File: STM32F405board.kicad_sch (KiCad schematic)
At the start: 24 parts

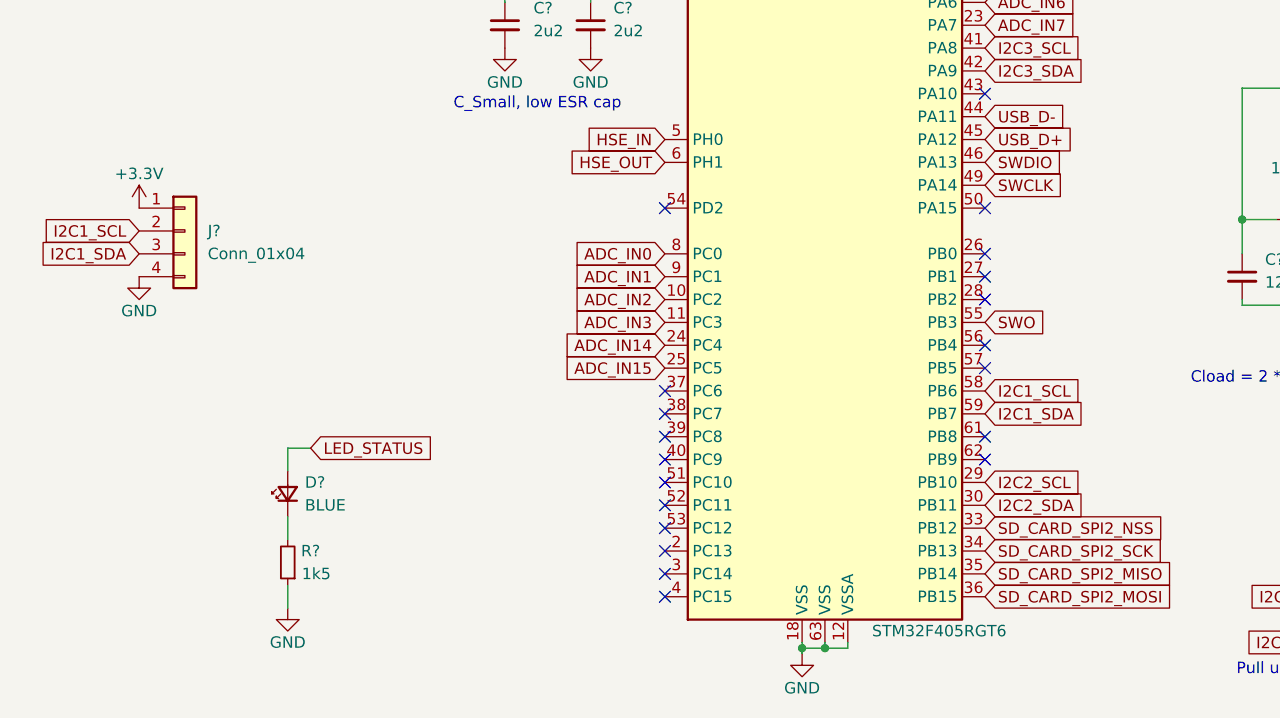
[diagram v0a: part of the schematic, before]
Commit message: Final Schematic
Final Schematic. PC104 pins not assigned.
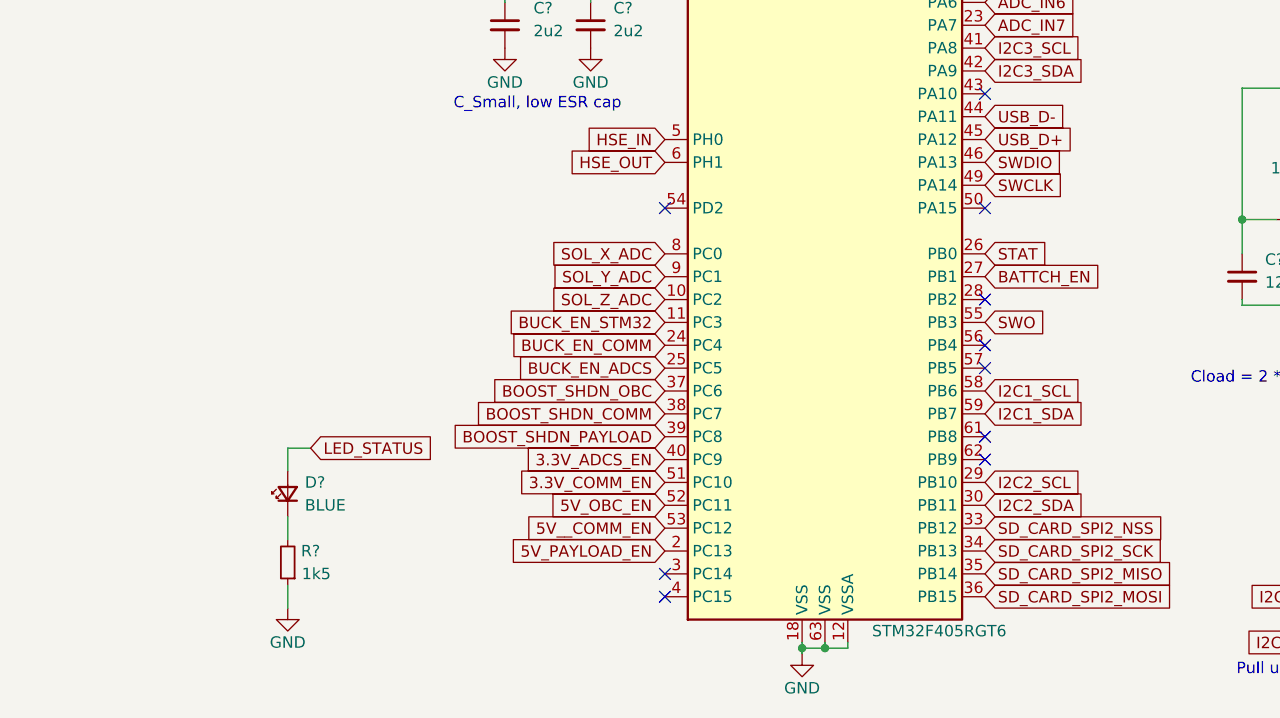
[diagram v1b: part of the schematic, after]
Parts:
- removed J?: Conn_01x04, Connector_Molex:Molex_PicoBlade_53048-0410_1x04_P1.25mm_Horizontal, symbol Connector_Generic:Conn_01x04
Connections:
- net 5V_PAYLOAD_EN: now reaches U?.2 (PC13)
- net STAT: now reaches U?.26 (PB0)
- net BATTCH_EN: now reaches U?.27 (PB1)
- net BOOST_SHDN_OBC: now reaches U?.37 (PC6)
- net BOOST_SHDN_COMM: now reaches U?.38 (PC7)
- net BOOST_SHDN_PAYLOAD: now reaches U?.39 (PC8)
- net 3.3V_ADCS_EN: now reaches U?.40 (PC9)
- net 3.3V_COMM_EN: now reaches U?.51 (PC10)
- net 5V_OBC_EN: now reaches U?.52 (PC11)
- net 5V__COMM_EN: now reaches U?.53 (PC12)
- net ADC_IN0 renamed SOL_X_ADC
- net ADC_IN1 renamed SOL_Y_ADC
- net ADC_IN14 renamed BUCK_EN_COMM
- net ADC_IN15 renamed BUCK_EN_ADCS
- net ADC_IN2 renamed SOL_Z_ADC
- net ADC_IN3 renamed BUCK_EN_STM32
- no-connect marks 24 -> 14

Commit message: Ready to rearrange
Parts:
- J?: footprint Connector_PinHeader_1.27mm:PinHeader_2x05_P1.27mm_Vertical_SMD -> Connector_PinHeader_1.00mm:PinHeader_2x05_P1.00mm_Vertical_SMD
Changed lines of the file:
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@@
       (effects (font (size 1.27 1.27)))
     )
-    (property "Footprint" "Connector_PinHeader_1.27mm:PinHeader_2x05_P1.27mm_Vertical_SMD" (at 233.68 100.33 0)
+    (property "Footprint" "Connector_PinHeader_1.00mm:PinHeader_2x05_P1.00mm_Vertical_SMD" (at 233.68 100.33 0)
       (effects (font (size 1.27 1.27)) hide)
     )

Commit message: updates
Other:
- moved on the sheet: J?
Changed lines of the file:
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@@
   (junction (at 127 61.595) (diameter 0) (color 0 0 0 0)
   )
-  (junction (at 226.695 100.33) (diameter 0) (color 0 0 0 0)
+  (junction (at 127.635 38.1) (diameter 0) (color 0 0 0 0)
   )
   (junction (at 132.08 154.305) (diameter 0) (color 0 0 0 0)
   )
-  (junction (at 226.695 105.41) (diameter 0) (color 0 0 0 0)
+  (junction (at 127.635 43.18) (diameter 0) (color 0 0 0 0)
   )
   (junction (at 134.62 61.595) (diameter 0) (color 0 0 0 0)
@@
   (junction (at 179.07 33.655) (diameter 0) (color 0 0 0 0)
   )
-  (no_connect (at 228.6 102.87))
+  (no_connect (at 129.54 40.64))
   (no_connect (at 149.86 130.81))
   (no_connect (at 149.86 120.65))
@@
   (no_connect (at 114.3 148.59))
   (no_connect (at 149.86 67.31))
-  (no_connect (at 241.3 102.87))
+  (no_connect (at 142.24 40.64))
   (no_connect (at 149.86 123.19))
   (no_connect (at 149.86 69.85))
@@
     (stroke (width 0) (type default))
   )
-  (wire (pts (xy 226.695 93.345) (xy 226.695 95.25))
+  (wire (pts (xy 127.635 31.115) (xy 127.635 33.02))
     (stroke (width 0) (type default))
   )
@@
     (stroke (width 0) (type default))
   )
-  (wire (pts (xy 226.695 95.25) (xy 228.6 95.25))
+  (wire (pts (xy 127.635 33.02) (xy 129.54 33.02))
     (stroke (width 0) (type default))
   )
@@
     (stroke (width 0) (type default))
   )
-  (wire (pts (xy 226.695 100.33) (xy 226.695 105.41))
+  (wire (pts (xy 127.635 38.1) (xy 127.635 43.18))
     (stroke (width 0) (type default))
   )
@@
     (stroke (width 0) (type default))
   )
-  (wire (pts (xy 228.6 97.79) (xy 226.695 97.79))
-    (stroke (width 0) (type default))
-  )
-  (wire (pts (xy 228.6 105.41) (xy 226.695 105.41))
+  (wire (pts (xy 129.54 35.56) (xy 127.635 35.56))
+    (stroke (width 0) (type default))
+  )
+  (wire (pts (xy 129.54 43.18) (xy 127.635 43.18))
     (stroke (width 0) (type default))
   )
@@
     (stroke (width 0) (type default))
   )
-  (wire (pts (xy 226.695 97.79) (xy 226.695 100.33))
+  (wire (pts (xy 127.635 35.56) (xy 127.635 38.1))
     (stroke (width 0) (type default))
   )
@@
     (stroke (width 0) (type default))
   )
-  (wire (pts (xy 226.695 105.41) (xy 226.695 107.315))
+  (wire (pts (xy 127.635 43.18) (xy 127.635 45.085))
     (stroke (width 0) (type default))
   )
@@
     (stroke (width 0) (type default))
   )
-  (wire (pts (xy 228.6 100.33) (xy 226.695 100.33))
+  (wire (pts (xy 129.54 38.1) (xy 127.635 38.1))
     (stroke (width 0) (type default))
   )
@@
     (effects (font (size 1.27 1.27)) (justify left bottom))
   )
-  (text "DEBUG connector" (at 228.6 116.84 0)
+  (text "DEBUG connector" (at 129.54 54.61 0)
     (effects (font (size 1.27 1.27)) (justify left bottom))
   )
@@
     )
   )
-  (global_label "SWDIO" (shape input) (at 241.3 95.25 0) (fields_autoplaced)
-    (effects (font (size 1.27 1.27)) (justify left))
-    (property "Intersheetrefs" "${INTERSHEET_REFS}" (at 4.445 20.955 0)
-      (effects (font (size 1.27 1.27)) hide)
-    )
-  )
-  (global_label "SWCLK" (shape input) (at 241.3 97.79 0) (fields_autoplaced)
-    (effects (font (size 1.27 1.27)) (justify left))
-    (property "Intersheetrefs" "${INTERSHEET_REFS}" (at 4.445 20.955 0)
+  (global_label "SWDIO" (shape input) (at 142.24 33.02 0) (fields_autoplaced)
+    (effects (font (size 1.27 1.27)) (justify left))
+    (property "Intersheetrefs" "${INTERSHEET_REFS}" (at -94.615 -41.275 0)
+      (effects (font (size 1.27 1.27)) hide)
+    )
+  )
+  (global_label "SWCLK" (shape input) (at 142.24 35.56 0) (fields_autoplaced)
+    (effects (font (size 1.27 1.27)) (justify left))
+    (property "Intersheetrefs" "${INTERSHEET_REFS}" (at -94.615 -41.275 0)
       (effects (font (size 1.27 1.27)) hide)
     )
@@
     )
   )
-  (global_label "NRST" (shape input) (at 241.3 105.41 0) (fields_autoplaced)
-    (effects (font (size 1.27 1.27)) (justify left))
-    (property "Intersheetrefs" "${INTERSHEET_REFS}" (at 4.445 20.955 0)
+  (global_label "NRST" (shape input) (at 142.24 43.18 0) (fields_autoplaced)
+    (effects (font (size 1.27 1.27)) (justify left))
+    (property "Intersheetrefs" "${INTERSHEET_REFS}" (at -94.615 -41.275 0)
       (effects (font (size 1.27 1.27)) hide)
     )
@@
     )
   )
-  (global_label "SWO" (shape input) (at 241.3 100.33 0) (fields_autoplaced)
-    (effects (font (size 1.27 1.27)) (justify left))
-    (property "Intersheetrefs" "${INTERSHEET_REFS}" (at 4.445 20.955 0)
+  (global_label "SWO" (shape input) (at 142.24 38.1 0) (fields_autoplaced)
+    (effects (font (size 1.27 1.27)) (justify left))
+    (property "Intersheetrefs" "${INTERSHEET_REFS}" (at -94.615 -41.275 0)
       (effects (font (size 1.27 1.27)) hide)
     )
@@
     )
   )
-  (symbol (lib_id "Connector_Generic:Conn_02x05_Odd_Even") (at 233.68 100.33 0) (unit 1)
-    (in_bom yes) (on_board yes) (dnp no)
-    (property "Reference" "J?" (at 234.95 92.71 0)
-      (effects (font (size 1.27 1.27)))
-    )
-    (property "Value" "SWD" (at 234.95 108.585 0)
-      (effects (font (size 1.27 1.27)))
-    )
-    (property "Footprint" "Connector_PinHeader_1.00mm:PinHeader_2x05_P1.00mm_Vertical_SMD" (at 233.68 100.33 0)
-      (effects (font (size 1.27 1.27)) hide)
-    )
-    (property "Datasheet" "~" (at 233.68 100.33 0)
+  (symbol (lib_id "Connector_Generic:Conn_02x05_Odd_Even") (at 134.62 38.1 0) (unit 1)
+    (in_bom yes) (on_board yes) (dnp no)
+    (property "Reference" "J?" (at 135.89 30.48 0)
+      (effects (font (size 1.27 1.27)))
+    )
+    (property "Value" "SWD" (at 135.89 46.355 0)
+      (effects (font (size 1.27 1.27)))
+    )
+    (property "Footprint" "Connector_PinHeader_1.00mm:PinHeader_2x05_P1.00mm_Vertical_SMD" (at 134.62 38.1 0)
+      (effects (font (size 1.27 1.27)) hide)
+    )
+    (property "Datasheet" "~" (at 134.62 38.1 0)
       (effects (font (size 1.27 1.27)) hide)
     )
@@
     )
   )
-  (symbol (lib_id "STM32F4_REV2-rescue:+3.3V-power") (at 226.695 93.345 0) (unit 1)
-    (in_bom yes) (on_board yes) (dnp no)
-    (property "Reference" "#PWR?" (at 226.695 97.155 0)
-      (effects (font (size 1.27 1.27)) hide)
-    )
-    (property "Value" "+3.3V" (at 226.695 89.535 0)
-      (effects (font (size 1.27 1.27)))
-    )
-    (property "Footprint" "" (at 226.695 93.345 0)
-      (effects (font (size 1.27 1.27)) hide)
-    )
-    (property "Datasheet" "" (at 226.695 93.345 0)
+  (symbol (lib_id "STM32F4_REV2-rescue:+3.3V-power") (at 127.635 31.115 0) (unit 1)
+    (in_bom yes) (on_board yes) (dnp no)
+    (property "Reference" "#PWR?" (at 127.635 34.925 0)
+      (effects (font (size 1.27 1.27)) hide)
+    )
+    (property "Value" "+3.3V" (at 127.635 27.305 0)
+      (effects (font (size 1.27 1.27)))
+    )
+    (property "Footprint" "" (at 127.635 31.115 0)
+      (effects (font (size 1.27 1.27)) hide)
+    )
+    (property "Datasheet" "" (at 127.635 31.115 0)
       (effects (font (size 1.27 1.27)) hide)
     )
@@
     )
   )
-  (symbol (lib_id "power:GND") (at 226.695 107.315 0) (unit 1)
-    (in_bom yes) (on_board yes) (dnp no)
-    (property "Reference" "#PWR?" (at 226.695 113.665 0)
-      (effects (font (size 1.27 1.27)) hide)
-    )
-    (property "Value" "GND" (at 226.695 111.125 0)
-      (effects (font (size 1.27 1.27)))
-    )
-    (property "Footprint" "" (at 226.695 107.315 0)
-      (effects (font (size 1.27 1.27)) hide)
-    )
-    (property "Datasheet" "" (at 226.695 107.315 0)
-      (effects (font (size 1.27 1.27)) hide)
-    )
+  (symbol (lib_id "power:GND") (at 127.635 45.085 0) (unit 1)
+    (in_bom yes) (on_board yes) (dnp no)
+    (property "Reference" "#PWR?" (at 127.635 51.435 0)
+      (effects (font (size 1.27 1.27)) hide)
+    )
+    (property "Value" "GND" (at 127.635 48.895 0)
+      (effects (font (size 1.27 1.27)))
+    )
+    (property "Footprint" "" (at 127.635 45.085 0)
+      (effects (font (size 1.27 1.27)) hide)
+    )
+    (property "Datasheet" "" (at 127.635 45.085 0)
+      (effects (font (size 1.27 1.27)) hide)
+    )
